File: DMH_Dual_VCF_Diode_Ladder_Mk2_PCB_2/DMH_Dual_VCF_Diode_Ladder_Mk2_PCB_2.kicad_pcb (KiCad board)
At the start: 2 copper layers, 146 x 175 mm, 201 parts, among them J0 Conn_01x01, J100 IDC_02x08, J50 Conn_01x06, J60 Conn_01x06, J70 Conn_01x06, J80 Conn_01x06, Q1 BC548, Q2 BC548, Q3 BC548, Q4 BC548, SW1 SW_SPDT, SW10 SW_DPDT_OnOn, SW2 SW_SPDT, SW3 SW_SPDT, SW4 SW_SPDT, SW5 SW_SPDT, SW6 SW_SPDT, SW7 SW_SPDT_OnOffOn, SW8 SW_SPDT_321, SW9 SW_SPDT_OnOffOn, U1 TL074, U2 TL074, U3 TL074, U4 TL074, U5 TL074, U6 TL074, U7 TL074

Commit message: Component placement on PCB2 in progress
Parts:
- removed C1, C2: 47uF, Capacitor_THT:CP_Radial_D5.0mm_P2.00mm
- removed C10, C11, C12, C13, C14, C15, C16, C17, C18, C3, C4, C5, C6, C7, C8, C9: 100nF, Capacitor_THT:C_Disc_D4.3mm_W1.9mm_P5.00mm
- removed C21, C27, C28, C34: 1uF, Capacitor_THT:C_Disc_D4.3mm_W1.9mm_P5.00mm
- removed C22, C23, C24, C25, C26, C29, C30, C31, C32, C33: 1nF, Capacitor_THT:C_Disc_D4.3mm_W1.9mm_P5.00mm
- removed D1: SB140+, Diode_THT:D_DO-41_SOD81_P10.16mm_Horizontal
- removed D10, D11, D12, D13, D14, D15, D16, D17, D18, D19, D20, D21, D22, D23, D6, D7, D8, D9: 1N4148, Diode_THT:D_DO-35_SOD27_P7.62mm_Horizontal
- removed D2: SB140-, Diode_THT:D_DO-41_SOD81_P10.16mm_Horizontal
- removed J0: Conn_01x01, Connector_PinHeader_2.54mm:PinHeader_1x01_P2.54mm_Vertical
- removed J100: IDC_02x08, SynthStuff:IDC-Header_2x08_P2.54mm_Vertical_Eurorack
- removed J50, J60, J70, J80: Conn_01x06, Connector_PinSocket_2.54mm:PinSocket_1x06_P2.54mm_Vertical
- removed Q1, Q2, Q3, Q4: BC548, Package_TO_SOT_THT:TO-92L_Inline_Wide
- removed R18, R21, R29, R3, R31, R32, R33, R34, R35, R36, R47, R49, R50, R51, R52, R53, R54, R6, R62, R79: 33k, Resistor_THT:R_Axial_DIN0207_L6.3mm_D2.5mm_P7.62mm_Horizontal
- removed R19, R22, R4, R7: 68k, Resistor_THT:R_Axial_DIN0207_L6.3mm_D2.5mm_P7.62mm_Horizontal
- removed R20, R5: 14k, Resistor_THT:R_Axial_DIN0207_L6.3mm_D2.5mm_P7.62mm_Horizontal
- removed R26, R28, R38, R42, R44, R46, R56, R60, R64, R65, R67, R71, R77, R81, R82, R84, R88, R93, R94: 100k, Resistor_THT:R_Axial_DIN0207_L6.3mm_D2.5mm_P7.62mm_Horizontal
- removed R27, R37, R55: 2k, Resistor_THT:R_Axial_DIN0207_L6.3mm_D2.5mm_P7.62mm_Horizontal
- removed R30, R48: 27k, Resistor_THT:R_Axial_DIN0207_L6.3mm_D2.5mm_P7.62mm_Horizontal
- removed R39, R40, R43, R57, R58, R61, R78, R95: 1k, Resistor_THT:R_Axial_DIN0207_L6.3mm_D2.5mm_P7.62mm_Horizontal
- removed R41, R59: 47K, Resistor_THT:R_Axial_DIN0207_L6.3mm_D2.5mm_P7.62mm_Horizontal
- removed R63, R72, R73, R89, R90: 20k, Resistor_THT:R_Axial_DIN0207_L6.3mm_D2.5mm_P7.62mm_Horizontal
- removed R66, R83: 82k, Resistor_THT:R_Axial_DIN0207_L6.3mm_D2.5mm_P7.62mm_Horizontal
- removed R68, R70, R85, R87: 100R, Resistor_THT:R_Axial_DIN0207_L6.3mm_D2.5mm_P7.62mm_Horizontal
- removed R69, R74, R75, R86, R91, R92: 10k, Resistor_THT:R_Axial_DIN0207_L6.3mm_D2.5mm_P7.62mm_Horizontal
- removed RV10, RV13, RV15, RV17, RV2, RV21, RV4, RV8: 50k, Potentiometer_THT:Potentiometer_Bourns_3296W_Vertical
- removed RV12, RV14: 100k, SynthStuff:Potentiometer_Alpha_RD901F-40-00D_Single_Vertical
- removed RV19, RV23: 100k, Potentiometer_THT:Potentiometer_Bourns_3296W_Vertical
- removed U1, U2, U3, U4, U5, U6, U7: TL074, Package_DIP:DIP-14_W7.62mm_Socket
- added J15: Conn_01x08_PinHeader, Connector_PinSocket_2.54mm:PinSocket_1x08_P2.54mm_Vertical, B.Cu at (30.0, 128.0)
- added J16: Conn_01x08_PinHeader, Connector_PinSocket_2.54mm:PinSocket_1x08_P2.54mm_Vertical, B.Cu at (170.0, 128.0)
- added J17: Conn_01x06_PinHeader, Connector_PinSocket_2.54mm:PinSocket_1x06_P2.54mm_Vertical, B.Cu at (30.0, 94.5)
- added J18: Conn_01x06_PinHeader, Connector_PinSocket_2.54mm:PinSocket_1x06_P2.54mm_Vertical, B.Cu at (170.0, 94.5)
- added J19: Conn_01x04_PinHeader, Connector_PinSocket_2.54mm:PinSocket_1x04_P2.54mm_Vertical, B.Cu at (98.0, 143.8)
- added J20: Conn_01x04_PinHeader, Connector_PinSocket_2.54mm:PinSocket_1x04_P2.54mm_Vertical, B.Cu at (102.0, 143.8)
- added J21: Conn_01x06_PinHeader, Connector_PinSocket_2.54mm:PinSocket_1x06_P2.54mm_Vertical, B.Cu at (30.0, 56.5)
- added J22: Conn_01x06_PinHeader, Connector_PinSocket_2.54mm:PinSocket_1x06_P2.54mm_Vertical, B.Cu at (170.0, 56.5)
- added J23: Conn_01x04_PinHeader, Connector_PinSocket_2.54mm:PinSocket_1x04_P2.54mm_Vertical, B.Cu at (96.2, 62.8)
- added R111: 20k, Resistor_THT:R_Axial_DIN0207_L6.3mm_D2.5mm_P7.62mm_Horizontal, F.Cu at (256.5, 169.4)
- added R128: 20k, Resistor_THT:R_Axial_DIN0207_L6.3mm_D2.5mm_P7.62mm_Horizontal, F.Cu at (263.5, 113.6)
- added RV25: 100k, SynthStuff:Potentiometer_TT_P110KH1, F.Cu at (60.2, 177.0)
- added RV27: 100k, SynthStuff:Potentiometer_Alpha_RD901F-40-00D_Single_Vertical, F.Cu at (42.5, 106.5)
- added RV28: 100k, SynthStuff:Potentiometer_TT_P110KH1, F.Cu at (134.8, 177.0)
- added RV30: 100k, SynthStuff:Potentiometer_Alpha_RD901F-40-00D_Single_Vertical, F.Cu at (152.5, 106.5)
- R1, R10, R11, R12, R13, R14, R15, R16, R17, R2, R23, R24, R25, R45, R8, R80, R9, R96: moved to F.Cu
- R76: value 100k -> 20k; moved to F.Cu
- SW8: value SW_SPDT_321 -> SW_DPDT_x2; footprint SynthStuff:Toggle_Switch_TE -> SynthStuff:Toggle_Switch_2_Poles_TE
- moved R76 225.4 mm to (273.9, 149.4), turned to 0 degrees
- moved R96 197.6 mm to (276.3, 113.6)
- moved R1 193.2 mm to (219.7, 113.6)
- moved R8 186.0 mm to (219.7, 121.7), turned to 0 degrees
- moved R2 175.1 mm to (219.7, 117.7), turned to 0 degrees
- moved R80 168.3 mm to (273.9, 168.8)
- moved R10 151.3 mm to (219.7, 129.8), turned to 0 degrees
- moved R9 148.8 mm to (219.7, 125.8), turned to 0 degrees
- moved R12 145.3 mm to (219.7, 137.9)
- moved R14 127.9 mm to (219.7, 146.0), turned to 0 degrees
- moved R11 127.4 mm to (219.7, 133.9), turned to 0 degrees
- moved R13 122.2 mm to (219.7, 142.0), turned to 0 degrees
- moved R17 121.3 mm to (219.7, 154.1), turned to 0 degrees
- moved R15 119.2 mm to (219.7, 150.1), turned to 0 degrees
- moved R25 109.3 mm to (219.7, 166.3), turned to 0 degrees
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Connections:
- R24 pad 2: /CV Processing/Bus CV A Input -> /CV Processing/CV3 B Input
- R76 pad 1: Net-(U1C-+) -> Net-(R76-Pad1)
- R76 pad 2: GND -> +12V
- R9 pad 2: /CV Processing/Bus CV A Input -> /CV Processing/CV3 A Input
- RV18 pad 3: Net-(R63-Pad1) -> Net-(R76-Pad1)
- SW10 pad 2: /CV Processing/Link Switch -> /CV Processing/Link CV Switch
- SW7 pad 3: /CV Processing/Bus CV A Input -> /CV Processing/CV3 A Input
- SW8 pad 1: /Core Circuit A/Output -> /Drive A/Drive CV
- SW8 pad 2: /Inputs and Outputs A/Feed Switch -> Net-(J18F-Pin_6)
- SW8 pad 3: /Core Circuit A/Input -> Net-(J18D-Pin_4)
- SW9 pad 3: /CV Processing/Bus CV A Input -> /CV Processing/CV3 B Input
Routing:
- net +12V: track 550.6 -> 0.00 mm
- net -12V: track 494.0 -> 0.00 mm
- net Net-(J15A-Pin_1): track 360.9 -> 0.00 mm
- net /Inputs and Outputs A/Res CV Jack: track 247.6 -> 0.00 mm
- net /CV Processing/Bus CV A Input: track 177.2 -> 0.00 mm
- net /Inputs and Outputs B/Res CV Jack: track 150.2 -> 0.00 mm
- net /Core Circuit A/Input: track 148.9 -> 0.00 mm
- net /CV Processing/CV2 A Input: track 147.5 -> 0.00 mm
- net Net-(D13-A): track 146.9 -> 0.00 mm
- net Net-(J21B-Pin_2): track 129.6 -> 0.00 mm
- net Net-(J22B-Pin_2): track 128.7 -> 0.00 mm
- net /CV Processing/CV B: track 117.8 -> 0.00 mm
- net /CV Processing/CV1 A Input: track 117.1 -> 0.00 mm
- net /CV Processing/Link Switch: track 115.9 -> 0.00 mm
- net /Core Circuit A/Output: track 113.9 -> 0.00 mm
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- removed copper zone on B.Cu, net GND
- removed copper zone on F.Cu, net GND
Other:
- outline, holes or cut-outs redrawn
- board text removed: "Mk1.0 - Month Year"

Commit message: pcb 2 routing in progress
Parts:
- removed R45: 2k, Resistor_THT:R_Axial_DIN0207_L6.3mm_D2.5mm_P7.62mm_Horizontal
- removed R96: 5M, Resistor_THT:R_Axial_DIN0207_L6.3mm_D2.5mm_P7.62mm_Horizontal
- R1, R10, R11, R111, R12, R128, R13, R14, R15, R16, R17, R2, R23, R24, R25, R76, R8, R80, R9: moved to B.Cu
- moved R111 228.8 mm to (41.2, 92.0)
- moved R76 202.8 mm to (76.2, 104.0)
- moved R8 182.7 mm to (37.2, 114.5)
- moved R10 182.6 mm to (37.2, 124.0)
- moved R1 177.2 mm to (52.8, 54.0), turned to 180 degrees
- moved R9 175.0 mm to (44.8, 119.2), turned to 180 degrees
- moved R80 170.4 mm to (116.2, 104.0)
- moved R2 169.7 mm to (57.2, 68.6), turned to 90 degrees
- moved R14 164.1 mm to (64.2, 93.8)
- moved R12 147.4 mm to (96.2, 57.5)
- moved R11 133.8 mm to (96.2, 82.5)
- moved R13 127.9 mm to (96.2, 108.8)
- moved R17 115.1 mm to (142.8, 68.6), turned to 90 degrees
- moved R15 107.5 mm to (128.2, 93.8)
- moved R128 106.9 mm to (158.8, 92.0), turned to 180 degrees
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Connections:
- J15 pad 2: /CV Processing/CV1 A Input -> /CV Processing/CV3 A Input
- J15 pad 3: Net-(J15C-Pin_3) -> /CV Processing/CV1 A Input
- J15 pad 4: /CV Processing/CV2 A Input -> Net-(J15D-Pin_4)
- J15 pad 5: Net-(J15E-Pin_5) -> /CV Processing/CV A
- J15 pad 6: /CV Processing/CV3 A Input -> /CV Processing/CV2 A Input
- J15 pad 7: /CV Processing/CV A -> Net-(J15G-Pin_7)
- J16 pad 2: /CV Processing/CV1 B Input -> /CV Processing/CV3 B Input
- J16 pad 4: /CV Processing/CV2 B Input -> /CV Processing/CV1 B Input
- J16 pad 5: Net-(J16E-Pin_5) -> /CV Processing/CV B
- J16 pad 6: /CV Processing/CV3 B Input -> /CV Processing/Link CV Switch
- J16 pad 7: /CV Processing/CV B -> Net-(J16G-Pin_7)
- J16 pad 8: /CV Processing/Link CV Switch -> /CV Processing/CV2 B Input
- J17 pad 1: /Drive A/Drive CV Input -> Net-(J17A-Pin_1)
- J17 pad 2: Net-(J17B-Pin_2) -> /Drive A/Drive CV Input
- J18 pad 1: /Drive B/Drive CV Input -> Net-(J18A-Pin_1)
- J18 pad 4: Net-(J18D-Pin_4) -> /Drive A/Drive CV
- J18 pad 5: /Drive A/Drive CV -> Net-(J18E-Pin_5)
- J18 pad 6: Net-(J18F-Pin_6) -> /Drive B/Drive CV Input
- J21 pad 1: /Inputs and Outputs A/Res CV Jack -> Net-(J21A-Pin_1)
- J21 pad 2: Net-(J21B-Pin_2) -> /Inputs and Outputs A/Res CV Jack
- J22 pad 1: /Inputs and Outputs B/Res CV Jack -> Net-(J22A-Pin_1)
- J22 pad 3: Net-(J22C-Pin_3) -> /Inputs and Outputs B/Res CV Jack
- J22 pad 5: /Resonance A CV/Res CV -> Net-(J22E-Pin_5)
- J22 pad 6: Net-(J22F-Pin_6) -> /Resonance A CV/Res CV
- RV11 pad 2: Net-(J16E-Pin_5) -> Net-(J16G-Pin_7)
- RV16 pad 2: Net-(J21B-Pin_2) -> Net-(J21C-Pin_3)
- RV18 pad 2: Net-(J21C-Pin_3) -> Net-(J21A-Pin_1)
- RV22 pad 2: Net-(J22C-Pin_3) -> Net-(J22A-Pin_1)
- RV25 pad 2: Net-(J17B-Pin_2) -> Net-(J17C-Pin_3)
- RV27 pad 2: Net-(J17C-Pin_3) -> Net-(J17A-Pin_1)
- RV28 pad 2: Net-(J18B-Pin_2) -> Net-(J18E-Pin_5)
- RV3 pad 2: Net-(J15C-Pin_3) -> Net-(J15D-Pin_4)
- RV30 pad 2: Net-(J18C-Pin_3) -> Net-(J18A-Pin_1)
- RV5 pad 2: Net-(J15E-Pin_5) -> Net-(J15G-Pin_7)
- SW8 pad 2: Net-(J18F-Pin_6) -> Net-(J18C-Pin_3)
- SW8 pad 3: Net-(J18D-Pin_4) -> Net-(J18B-Pin_2)
- SW8 pad 5: Net-(J22F-Pin_6) -> Net-(J22E-Pin_5)
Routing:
- net +12V: track 0.00 -> 327.9 mm
- net Net-(J15A-Pin_1): track 0.00 -> 200.8 mm
- net -12V: track 0.00 -> 90.2 mm
- net Net-(R14-Pad1): track 0.00 -> 65.9 mm
- net Net-(J20B-Pin_2): track 0.00 -> 35.5 mm
- net Net-(J19B-Pin_2): track 0.00 -> 35.5 mm
- net Net-(J19A-Pin_1): track 0.00 -> 34.4 mm
- net Net-(J20A-Pin_1): track 0.00 -> 34.4 mm
- net Net-(R12-Pad1): track 0.00 -> 22.4 mm
- net Net-(J20C-Pin_3): track 0.00 -> 22.3 mm
- net Net-(J19C-Pin_3): track 0.00 -> 22.3 mm
- net Net-(R80-Pad1): track 0.00 -> 17.1 mm
- net Net-(R76-Pad1): track 0.00 -> 17.1 mm
- net Net-(R16-Pad1): track 0.00 -> 16.1 mm
- net Net-(R1-Pad1): track 0.00 -> 16.1 mm
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- added copper zone on B.Cu, net GND
- added copper zone on F.Cu, net GND

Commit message: Finished PCB 2
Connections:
- J22 pad 3: /Inputs and Outputs B/Res CV Jack -> Net-(J22C-Pin_3)
- J22 pad 4: Net-(J22D-Pin_4) -> /Resonance A CV/Res CV
- J22 pad 6: /Resonance A CV/Res CV -> /Inputs and Outputs B/Res CV Jack
- RV20 pad 2: Net-(J22B-Pin_2) -> Net-(J22E-Pin_5)
- SW8 pad 5: Net-(J22E-Pin_5) -> Net-(J22C-Pin_3)
- SW8 pad 6: Net-(J22D-Pin_4) -> Net-(J22B-Pin_2)
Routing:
- net Net-(J18B-Pin_2): track 0.00 -> 168.8 mm
- net Net-(J18C-Pin_3): track 0.00 -> 162.5 mm
- net /Resonance A CV/Res CV: track 0.00 -> 159.5 mm
- net Net-(J22C-Pin_3): track 0.00 -> 158.4 mm
- net /Drive A/Drive CV: track 0.00 -> 156.3 mm
- net Net-(J22B-Pin_2): track 0.00 -> 156.2 mm
- net /Inputs and Outputs A/Res CV Jack: track 0.00 -> 146.9 mm
- net Net-(R14-Pad1): track 65.9 -> 212.2 mm
- net Net-(J21C-Pin_3): track 0.00 -> 143.4 mm
- net Net-(J22E-Pin_5): track 0.00 -> 134.7 mm
- net /CV Processing/CV A: track 0.00 -> 132.2 mm
- net /Inputs and Outputs B/Res CV Jack: track 0.00 -> 131.1 mm
- net /CV Processing/Link CV Switch: track 0.00 -> 121.0 mm
- net /CV Processing/CV B: track 0.00 -> 114.2 mm
- net Net-(J18E-Pin_5): track 0.00 -> 112.3 mm
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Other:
- board text added: "Mk2.0 - Month Year"

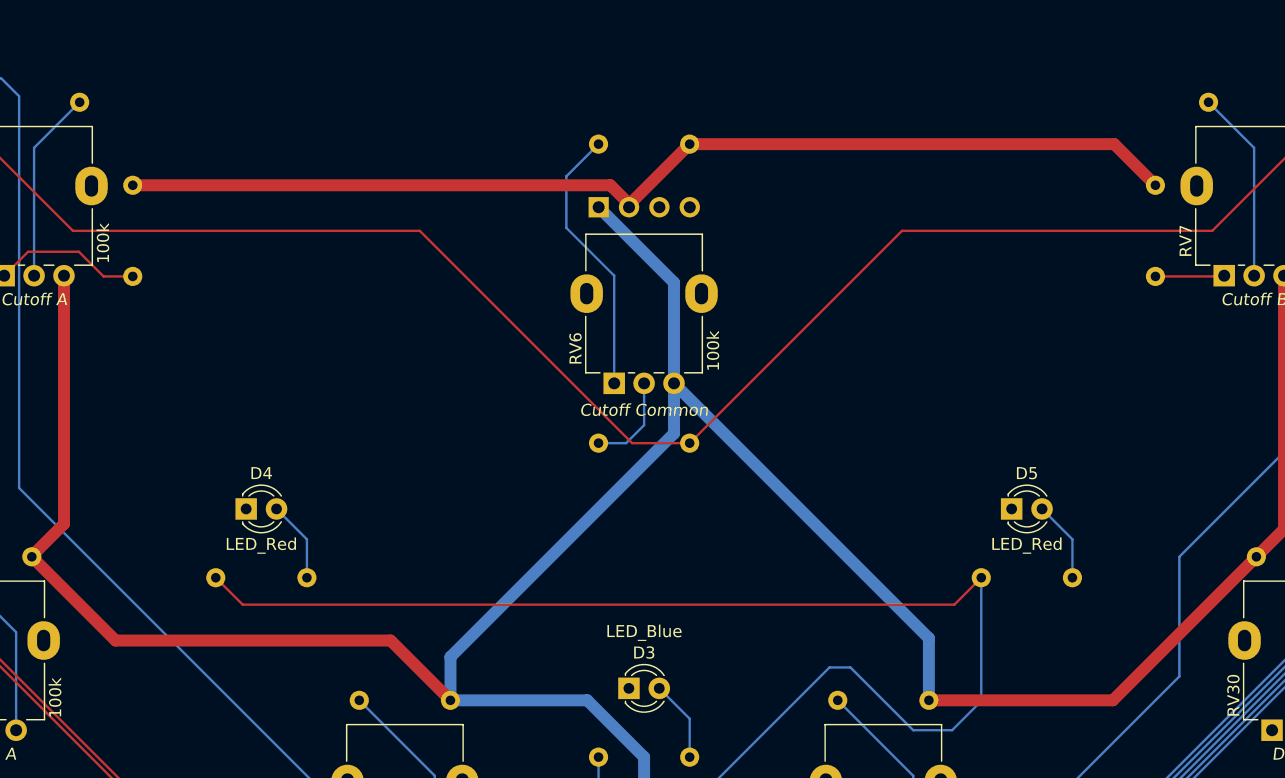
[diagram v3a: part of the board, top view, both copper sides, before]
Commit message: Replaced Central Cutoff pot with dual port
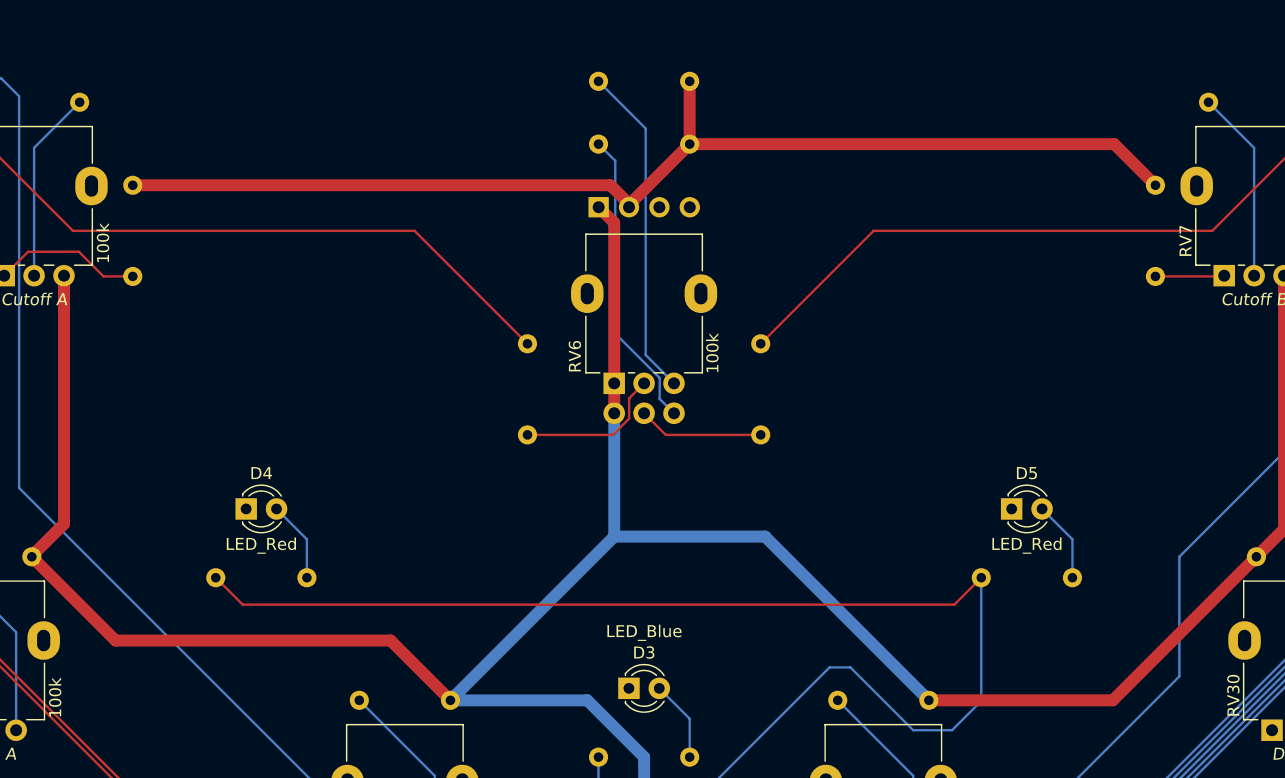
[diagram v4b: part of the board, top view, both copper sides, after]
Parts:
- added R131: 100k, Resistor_THT:R_Axial_DIN0207_L6.3mm_D2.5mm_P7.62mm_Horizontal, B.Cu at (109.8, 81.8)
- added R132: 27k, Resistor_THT:R_Axial_DIN0207_L6.3mm_D2.5mm_P7.62mm_Horizontal, B.Cu at (96.2, 52.2)
- RV6: footprint SynthStuff:Potentiometer_Alpha_RD901F-40-00D_Single_Vertical -> Potentiometer_THT:Potentiometer_Alpha_RD902F-40-00D_Dual_Vertical
- moved R11 5.98 mm to (90.2, 81.8), turned to 90 degrees
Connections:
- J16 pad 1: Net-(J15A-Pin_1) -> Net-(J16A-Pin_1)
- R16 pad 2: Net-(J15A-Pin_1) -> Net-(J16A-Pin_1)
- R23 pad 1: Net-(J15A-Pin_1) -> Net-(J16A-Pin_1)
- RV6 pad 1: Net-(R12-Pad1) -> +12V
- RV6 pad 3: +12V -> Net-(R132-Pad1)
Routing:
- net Net-(J15A-Pin_1): track 298.0 -> 135.9 mm
- net Net-(J16A-Pin_1): track 0.00 -> 135.8 mm
- net Net-(R132-Pad1): track 0.00 -> 27.9 mm
- net Net-(R131-Pad1): track 0.00 -> 10.5 mm
- net +12V: track 334.6 -> 327.1 mm
- net -12V: track 90.2 -> 95.4 mm
- net Net-(R11-Pad1): track 7.93 -> 12.5 mm
- net Net-(R12-Pad1): track 22.8 -> 25.1 mm

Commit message: Added buffering to each CV 3 input separately
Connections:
- net /CV Processing/CV3 A Input renamed Net-(J15B-Pin_2)
- net /CV Processing/CV3 B Input renamed Net-(J16B-Pin_2)

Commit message: Updated PCB 2 with validated features
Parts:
- removed R25, R9: 47k, Resistor_THT:R_Axial_DIN0207_L6.3mm_D2.5mm_P7.62mm_Horizontal
- added R135: 33k, Resistor_THT:R_Axial_DIN0207_L6.3mm_D2.5mm_P7.62mm_Horizontal, F.Cu at (71.2, 62.5)
- added R136: 47k, Resistor_THT:R_Axial_DIN0207_L6.3mm_D2.5mm_P7.62mm_Horizontal, F.Cu at (121.2, 57.5)
- added R137: 33k, Resistor_THT:R_Axial_DIN0207_L6.3mm_D2.5mm_P7.62mm_Horizontal, F.Cu at (121.2, 62.5)
- added R138: 47k, Resistor_THT:R_Axial_DIN0207_L6.3mm_D2.5mm_P7.62mm_Horizontal, F.Cu at (96.2, 54.2)
- added R139: 33k, Resistor_THT:R_Axial_DIN0207_L6.3mm_D2.5mm_P7.62mm_Horizontal, F.Cu at (101.2, 86.8)
- added R140: 10k, Resistor_THT:R_Axial_DIN0207_L6.3mm_D2.5mm_P7.62mm_Horizontal, F.Cu at (87.5, 63.8)
- added R141: 33k, Resistor_THT:R_Axial_DIN0207_L6.3mm_D2.5mm_P7.62mm_Horizontal, F.Cu at (91.2, 86.8)
- added R40: 1k, Resistor_THT:R_Axial_DIN0207_L6.3mm_D2.5mm_P7.62mm_Horizontal, F.Cu at (58.7, 117.8)
- added R58: 1k, Resistor_THT:R_Axial_DIN0207_L6.3mm_D2.5mm_P7.62mm_Horizontal, F.Cu at (140.7, 117.8)
- added R96: 47k, Resistor_THT:R_Axial_DIN0207_L6.3mm_D2.5mm_P7.62mm_Horizontal, F.Cu at (78.8, 57.5)
- added RV13: 50k, Potentiometer_THT:Potentiometer_Bourns_3296W_Vertical, F.Cu at (60.0, 123.9)
- added RV15: 50k, Potentiometer_THT:Potentiometer_Bourns_3296W_Vertical, F.Cu at (142.0, 123.9)
- added RV19: 100k, Potentiometer_THT:Potentiometer_Bourns_3296W_Vertical, F.Cu at (51.7, 152.2)
- added RV31: 100k, Potentiometer_THT:Potentiometer_Bourns_3296W_Vertical, F.Cu at (150.7, 152.2)
- J19, J20: value Conn_01x04_PinHeader -> Conn_01x06_PinHeader; footprint Connector_PinSocket_2.54mm:PinSocket_1x04_P2.54mm_Vertical -> Connector_PinSocket_2.54mm:PinSocket_1x06_P2.54mm_Vertical
- R1, R11, R111, R128, R13, R131, R14, R15, R16, R23, R76, R8, R80: moved to F.Cu
- R10, R24: value 47k -> 68k; moved to F.Cu
- R12: value 27k -> 47k; moved to F.Cu
- R132, R17, R2: value 27k -> 10k; moved to F.Cu
- moved R132 20.0 mm to (112.5, 63.8), turned to 90 degrees
- moved R11 7.62 mm to (90.2, 74.2), turned to -90 degrees
- moved R131 7.62 mm to (109.8, 74.2), turned to -90 degrees
- moved R10 4.75 mm to (37.2, 119.2)
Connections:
- R10 pad 1: GND -> Net-(SW7-A)
- R10 pad 2: Net-(SW7-A) -> Net-(SW7-C)
- R132 pad 2: -12V -> Net-(R132-Pad2)
- R17 pad 2: -12V -> Net-(R136-Pad2)
- R2 pad 2: -12V -> Net-(R2-Pad2)
- R24 pad 2: Net-(J16B-Pin_2) -> Net-(SW9-C)
- RV1 pad 3: +12V -> Net-(R135-Pad1)
- RV6 pad 1: +12V -> Net-(R132-Pad1)
- RV6 pad 3: Net-(R132-Pad1) -> Net-(R139-Pad1)
- RV6 pad 4: +12V -> Net-(R140-Pad1)
- RV6 pad 6: Net-(R12-Pad1) -> Net-(R141-Pad2)
- RV7 pad 3: +12V -> Net-(R137-Pad2)
- SW7 pad 3: Net-(J15B-Pin_2) -> Net-(SW7-C)
- SW9 pad 3: Net-(J16B-Pin_2) -> Net-(SW9-C)
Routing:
- net Net-(SW9-C): track 0.00 -> 94.4 mm
- net Net-(SW7-C): track 0.00 -> 82.1 mm
- net Net-(J15B-Pin_2): track 106.6 -> 33.8 mm
- net Net-(J16B-Pin_2): track 100.0 -> 32.9 mm
- net Net-(J20E-Pin_5): track 0.00 -> 44.0 mm
- net -12V: track 95.4 -> 52.1 mm
- net Net-(J19E-Pin_5): track 0.00 -> 42.1 mm
- net Net-(R137-Pad2): track 0.00 -> 29.7 mm
- net Net-(R140-Pad1): track 0.00 -> 23.4 mm
- net Net-(R135-Pad1): track 0.00 -> 22.2 mm
- net Net-(R132-Pad2): track 0.00 -> 19.2 mm
- net Net-(R12-Pad1): track 25.1 -> 9.23 mm
- net Net-(R2-Pad2): track 0.00 -> 15.4 mm
- net Net-(R136-Pad2): track 0.00 -> 15.4 mm
- net Net-(R139-Pad1): track 0.00 -> 11.0 mm
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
